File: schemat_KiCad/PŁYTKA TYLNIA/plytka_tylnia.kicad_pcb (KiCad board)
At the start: 2 copper layers, 113.5 x 70.2 mm, 36 parts, among them P1 USB_OTG, SW1 SPST

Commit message: tył do druku
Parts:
- removed BUTTON1: PUSH, warsztatymisc:SW_06_SMD
- removed R4: 10k, Resistors_SMD:R_0805_HandSoldering
- removed R5: 200, Resistors_SMD:R_0805_HandSoldering
- removed SW1: SPST, warsztatymisc:dip_switch_1
- removed SYGNAL_LED1: LED_BLUE, LEDs:LED_0805
- added BOOT0: SWITCH, warsztaty:PRZEŁĄCZNIK_1x3, F.Cu at (94.8, 94.0)
- added Bezpiecznik1: Fuse ??, Fuse_Holders_and_Fuses:Fuse_SMD1206_HandSoldering, B.Cu at (102.4, 87.2)
- added C1: 4,7uF, Capacitors_SMD:C_0805_HandSoldering, F.Cu at (160.9, 74.0)
- added C12: 100nF, Capacitors_SMD:C_0805_HandSoldering, F.Cu at (159.5, 71.8)
- added C15: 10uF, Capacitors_SMD:C_0805_HandSoldering, F.Cu at (113.6, 74.1)
- added C16: 10uF, Capacitors_SMD:C_0805_HandSoldering, F.Cu at (116.8, 64.5)
- added C17: C, Capacitors_SMD:C_0805_HandSoldering, F.Cu at (123.8, 66.9)
- added J1: CONN_01X04, Pin_Headers:Pin_Header_Straight_1x04_Pitch2.00mm, F.Cu at (121.5, 63.3)
- added J2: PIN8, Pin_Headers:Pin_Header_Straight_1x08_Pitch2.00mm, F.Cu at (110.0, 124.0)
- added J3: PIN8, Pin_Headers:Pin_Header_Straight_1x08_Pitch2.00mm, F.Cu at (165.0, 110.0)
- added LED_RGB1: LED_CRGB, warsztaty:LED_RGB_0805, F.Cu at (172.9, 56.9)
- added R10: R, Resistors_SMD:R_0805_HandSoldering, F.Cu at (178.2, 57.0)
- added R11: R, Resistors_SMD:R_0805_HandSoldering, F.Cu at (174.3, 61.1)
- added R12: R, Resistors_SMD:R_0805_HandSoldering, F.Cu at (172.2, 61.1)
- added R13: R, Resistors_SMD:R_0805_HandSoldering, F.Cu at (170.2, 61.1)
- added R7: 51k, Resistors_SMD:R_0805_HandSoldering, B.Cu at (95.8, 82.4)
- added R8: 33k, Resistors_SMD:R_0805_HandSoldering, B.Cu at (94.2, 86.9)
- added REF**: Napęd_tunelowy, Napęd_tunelowy, F.Cu at (137.7, 94.9)
- added REF**: Silnik Pololu, warsztaty:Pololu_silnik, F.Cu at (187.5, 117.5)
- added REF**: Silnik Pololu, warsztaty:Pololu_silnik, F.Cu at (87.5, 117.5)
- added SHARP1: PIN3, Pin_Headers:Pin_Header_Straight_1x03_Pitch2.00mm, F.Cu at (90.0, 73.0)
- added SHARP_RIGHT1: PIN3, Pin_Headers:Pin_Header_Straight_1x03_Pitch2.00mm, F.Cu at (185.0, 69.0)
- added STABILIZATOR2: LM1117DT, warsztaty:LM1117_TO-252, F.Cu at (108.2, 75.9)
- added SWITCH1: Przełącznik_dźwigniowy_podwójny_On-On_MTS, warsztaty:PRZEŁĄCZNIK_2x3, F.Cu at (175.3, 104.7)
- added TURBINA1: PIN3, Pin_Headers:Pin_Header_Straight_1x03_Pitch2.00mm, F.Cu at (91.1, 108.9)
- added Włącznik1: switch, warsztaty:PRZEŁĄCZNIK_1x2, F.Cu at (103.0, 98.8)
- BATERIA1: footprint warsztatymisc:zl_zasilania -> misc:zl_zasilania
- BLUETOOTH1: footprint warsztatymisc:pin_array_4x1 -> Pin_Headers:Pin_Header_Straight_1x04_Pitch2.00mm
- C13, C14, C2, C3, C8, C9, R6, STABILIZATOR1: moved to B.Cu
- C5: footprint warsztatymisc:1206 -> Capacitors_SMD:C_0805_HandSoldering
- C7: footprint warsztatymisc:1210 -> Capacitors_SMD:C_0805_HandSoldering
- MIKROPROCEK1: footprint warsztatymisc:LQFP48 -> misc:LQFP48
- MOTOR_L2, MOTOR_R1: footprint warsztatymisc:silnik -> Pin_Headers:Pin_Header_Straight_1x02_Pitch2.00mm
- P1: footprint warsztatymisc:USB-MINI-B-SMD -> Connectors_USB:USB_Micro-B_Molex-105017-0001
- PRZYCISK_RESET1, START_BUTTON1: footprint warsztatymisc:SW_06_SMD -> misc:SW_06_SMD
- REZONATOR1: footprint warsztatymisc:Kwarc_SMD_Mini -> misc:Kwarc_SMD_Mini; moved to B.Cu
- TRANSISTOR1: footprint warsztatymisc:SOT23-3 -> misc:SOT23-3; moved to B.Cu
- WYJSCIE_DO_PLYTKI_PRZEDNIEJ1: footprint warsztatymisc:fpc_10_pin -> misc:fpc_10_pin
- moved P1 79.5 mm to (94.8, 60.8), turned to 270 degrees
- moved R2 69.3 mm to (100.5, 54.1)
- moved PRZYCISK_RESET1 67.2 mm to (98.7, 87.3)
- moved R3 61.5 mm to (178.9, 79.4), turned to 180 degrees
- moved START_BUTTON1 61.1 mm to (179.7, 86.8), turned to 270 degrees
- moved BLUETOOTH1 55.6 mm to (111.5, 57.8)
- moved C6 52.9 mm to (177.8, 61.8), turned to 0 degrees
- moved BATERIA1 51.4 mm to (120.0, 124.0)
- moved LED_VCC_BATERY1 47.9 mm to (159.9, 56.4), turned to 180 degrees
- moved C13 44.3 mm to (171.5, 79.3)
- moved C14 43.9 mm to (173.9, 79.2)
- moved C10 42.0 mm to (163.1, 78.3)
- moved R1 41.0 mm to (157.4, 60.0), turned to 90 degrees
- moved C11 40.6 mm to (163.7, 80.2)
- moved C9 37.3 mm to (99.5, 76.6)
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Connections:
- BATERIA1 pad 1: Net-(BATERIA1-Pad1) -> GND
- BLUETOOTH1 pad 2: /USART_TX -> /SWCLK
- C2 pad 1: Net-(C3-Pad1) -> Net-(C2-Pad1)
- C3 pad 1: Net-(C2-Pad1) -> Net-(C3-Pad1)
- MIKROPROCEK1 pad 18: Net-(MIKROPROCEK1-Pad45) -> /SHARP_LEFT
- MIKROPROCEK1 pad 19: (no net) -> /LIPOL_POMIAR
- MIKROPROCEK1 pad 2: (no net) -> /LED_R
- MIKROPROCEK1 pad 20: Net-(MIKROPROCEK1-Pad20) -> (no net)
- MIKROPROCEK1 pad 21: (no net) -> /TURBINA_PWM
- MIKROPROCEK1 pad 3: (no net) -> /LED_G
- MIKROPROCEK1 pad 33: (no net) -> Net-(MIKROPROCEK1-Pad33)
- MIKROPROCEK1 pad 38: (no net) -> /USART_RX
- MIKROPROCEK1 pad 39: (no net) -> /SPI1_CLK
- MIKROPROCEK1 pad 4: (no net) -> /LED_B
- MIKROPROCEK1 pad 40: (no net) -> /SPI1_MISO
- MIKROPROCEK1 pad 41: Net-(BUTTON1-Pad2) -> /SPI1_MOSI
- MIKROPROCEK1 pad 42: /USART_RX -> /SPI1_SS1
- MIKROPROCEK1 pad 43: /USART_TX -> /SPI1_SS2
- MIKROPROCEK1 pad 44: (no net) -> /BOOT0
- MIKROPROCEK1 pad 46: (no net) -> /SHARP_RIGHT
- MIKROPROCEK1 pad 5: Net-(C2-Pad1) -> /OSC_IN
- MIKROPROCEK1 pad 6: Net-(C3-Pad1) -> (no net)
- R3 pad 2: Net-(MIKROPROCEK1-Pad20) -> Net-(MIKROPROCEK1-Pad33)
- R6 pad 1: Net-(C8-Pad1) -> /BATERIA
- R6 pad 2: /BATERIA -> Net-(R6-Pad2)
- REZONATOR1 pad 1: Net-(C2-Pad1) -> Net-(C3-Pad1)
- REZONATOR1 pad 2: Net-(C3-Pad1) -> Net-(C2-Pad1)
- START_BUTTON1 pad 2: Net-(MIKROPROCEK1-Pad20) -> Net-(MIKROPROCEK1-Pad33)
- TRANSISTOR1 pad 1: Net-(C8-Pad1) -> GND
- TRANSISTOR1 pad 2: GND -> Net-(R6-Pad2)
- TRANSISTOR1 pad 3: Net-(BATERIA1-Pad1) -> GND
- WYJSCIE_DO_PLYTKI_PRZEDNIEJ1 pad 1: /T8 -> /T1
- WYJSCIE_DO_PLYTKI_PRZEDNIEJ1 pad 2: /T7 -> /T2
- WYJSCIE_DO_PLYTKI_PRZEDNIEJ1 pad 3: /T6 -> /T3
- WYJSCIE_DO_PLYTKI_PRZEDNIEJ1 pad 4: /T5 -> /T4
- WYJSCIE_DO_PLYTKI_PRZEDNIEJ1 pad 5: /T4 -> /T5
- WYJSCIE_DO_PLYTKI_PRZEDNIEJ1 pad 6: /T3 -> /T6
- WYJSCIE_DO_PLYTKI_PRZEDNIEJ1 pad 7: /T2 -> /T7
- WYJSCIE_DO_PLYTKI_PRZEDNIEJ1 pad 8: /T1 -> /T8
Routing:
- net /5V: track 0.00 -> 333.5 mm, vias 0 -> 1
- net GND: track 444.1 -> 156.8 mm, vias 2 -> 1
- net /SPI1_SS1: track 0.00 -> 227.1 mm, vias 0 -> 1
- net VCC: track 205.5 -> 426.5 mm, vias 3 -> 5
- net /SPI1_MISO: track 0.00 -> 186.0 mm, vias 0 -> 2
- net /SPI1_CLK: track 0.00 -> 160.4 mm, vias 0 -> 2
- net /BOOT0: track 0.00 -> 150.0 mm, vias 0 -> 1
- net /SPI1_MOSI: track 0.00 -> 148.8 mm, vias 0 -> 3
- net /BATERIA: track 71.2 -> 219.8 mm, vias 2 -> 3
- net Net-(MOSTEK1-Pad1): track 7.59 -> 135.5 mm, vias 0 -> 1
- net Net-(MOSTEK1-Pad5): track 12.9 -> 128.3 mm, vias 0 -> 3
- net /TURBINA_PWM: track 0.00 -> 99.3 mm, vias 0 -> 2
- net /TRIG: track 0.00 -> 87.2 mm
- net /SHARP_LEFT: track 0.00 -> 84.2 mm, vias 0 -> 4
- net /LIPOL_POMIAR: track 0.00 -> 82.6 mm, vias 0 -> 1
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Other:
- board size 113.5 x 70.2 mm -> 135 x 101 mm
- board text added: "L.F. ANT"
- board text removed: "BEBO"

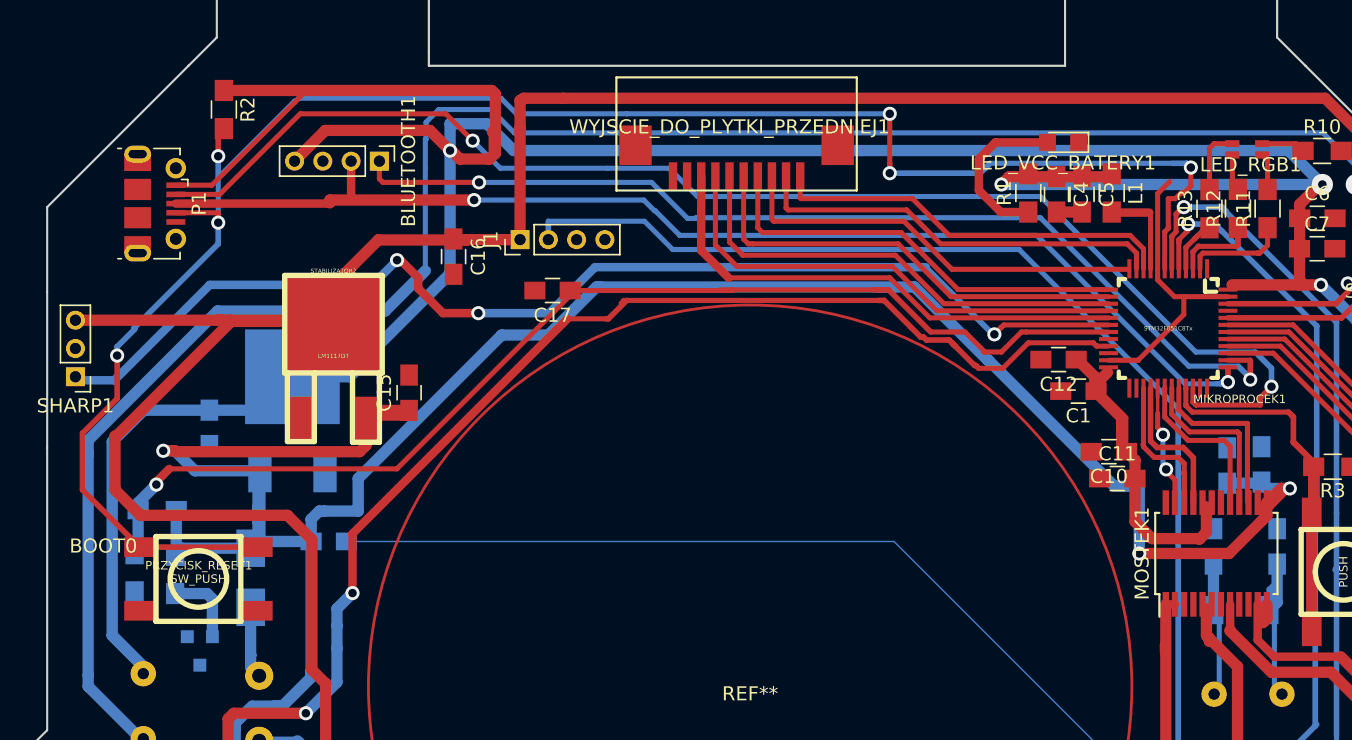
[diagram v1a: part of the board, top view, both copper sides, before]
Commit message: nazwy przyciskow
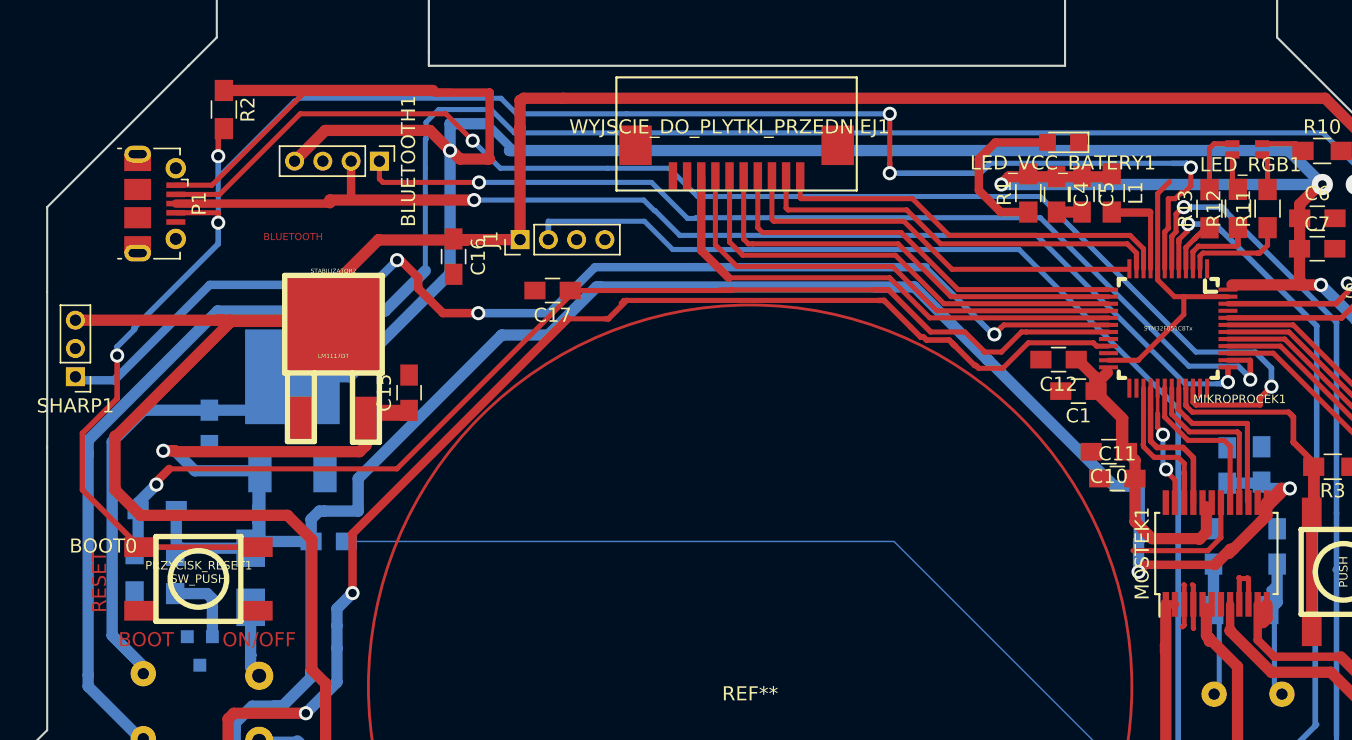
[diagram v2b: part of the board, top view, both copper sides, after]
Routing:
- net GND: track 156.8 -> 176.6 mm
- net VCC: track 426.5 -> 423.3 mm
- net /BATERIA: track 219.8 -> 222.2 mm
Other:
- board text added: "BLUETOOTH"
- board text added: "BOOT"
- board text added: "ON/OFF"
- board text added: "RESET"

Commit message: warstwa dolna okrag
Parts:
- added REF**: Napęd_tunelowy, warsztaty:Napęd_tunelowy, B.Cu at (137.7, 94.9)
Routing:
- net Net-(MOSTEK1-Pad5): track 128.3 -> 138.3 mm
- net Net-(MOSTEK1-Pad1): track 135.5 -> 127.3 mm
- net /5V: track 333.5 -> 331.1 mm
- net /SPI1_CLK: track 160.4 -> 161.2 mm
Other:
- outline, holes or cut-outs redrawn

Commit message: wejscie turbiny tylem
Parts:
- moved TURBINA1 68.9 mm to (157.2, 128.2)
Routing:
- net /ECHO: track 0.14 -> 82.9 mm
- net (no net): track 60.3 -> 108.1 mm
- net /OSC_IN: track 47.8 -> 90.1 mm
- net GND: track 176.6 -> 140.0 mm, vias 1 -> 2
- net /BATERIA: track 222.2 -> 254.4 mm, vias 3 -> 4
- net Net-(MOSTEK1-Pad5): track 138.3 -> 117.9 mm
- net /TURBINA_PWM: track 99.3 -> 80.7 mm
- net /SPI1_MISO: track 186.0 -> 193.2 mm
- net VCC: track 423.3 -> 416.8 mm
- net Net-(C2-Pad1): track 12.6 -> 18.9 mm
- net Net-(C3-Pad1): track 8.94 -> 14.9 mm
- net /TRIG: track 87.2 -> 92.1 mm
- net /SPI1_SS1: track 227.1 -> 222.8 mm
- net Net-(MIKROPROCEK1-Pad33): track 29.5 -> 26.2 mm
- net /SPI1_MOSI: track 148.8 -> 151.3 mm
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
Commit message: poprawiony echo/trig
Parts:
- removed SWITCH1: Przełącznik_dźwigniowy_podwójny_On-On_MTS, warsztaty:PRZEŁĄCZNIK_2x3
- added R14: R, Resistors_SMD:R_0805_HandSoldering, B.Cu at (169.7, 77.5)
- added R15: R, Resistors_SMD:R_0805_HandSoldering, B.Cu at (169.7, 82.4)
- added R4: R, Resistors_SMD:R_0805_HandSoldering, F.Cu at (176.8, 55.9)
- added R5: R, Resistors_SMD:R_0805_HandSoldering, F.Cu at (170.2, 58.2)
- added R9: R, Resistors_SMD:R_0805_HandSoldering, F.Cu at (168.1, 56.1)
- moved BOOT0 74.6 mm to (169.4, 93.9)
- moved REZONATOR1 27.7 mm to (169.5, 61.9)
- moved C2 21.9 mm to (174.9, 63.1), turned to 270 degrees
- moved C3 18.5 mm to (170.7, 66.5), turned to 270 degrees
- moved START_BUTTON1 9.67 mm to (179.0, 96.4)
- moved LED_VCC_BATERY1 9.49 mm to (150.4, 56.4), turned to 0 degrees
- moved C4 7.27 mm to (152.1, 59.7)
- moved L1 7.09 mm to (156.2, 59.9)
- moved R13 7.06 mm to (166.1, 55.4)
- moved C5 7.03 mm to (154.2, 59.7)
- moved R1 4.37 mm to (154.9, 56.4), turned to 0 degrees
- moved R10 4.14 mm to (175.3, 54.1)
- moved LED_RGB1 3.63 mm to (170.9, 53.8)
- moved C9 3.44 mm to (100.1, 73.2)
- moved R12 2.93 mm to (172.2, 58.2)
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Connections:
- MIKROPROCEK1 pad 35: (no net) -> Net-(MIKROPROCEK1-Pad35)
- MIKROPROCEK1 pad 36: (no net) -> /TRIG
- MIKROPROCEK1 pad 5: /OSC_IN -> Net-(C2-Pad1)
- MIKROPROCEK1 pad 6: (no net) -> Net-(C3-Pad1)
- R13 pad 1: /LED_B -> GND
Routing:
- net /BOOT0: track 150.0 -> 42.1 mm
- net /OSC_IN: track 90.1 -> 0.00 mm, vias 1 -> 0
- net (no net): track 108.1 -> 19.1 mm, vias 1 -> 0
- net GND: track 140.0 -> 223.5 mm, vias 2 -> 0
- net VCC: track 416.8 -> 368.0 mm, vias 5 -> 7
- net /ECHO: track 82.9 -> 52.9 mm
- net /TRIG: track 92.1 -> 64.4 mm, vias 0 -> 1
- net /BATERIA: track 254.4 -> 278.2 mm, vias 4 -> 5
- net /SWCLK: track 108.4 -> 87.6 mm
- net /5V: track 330.8 -> 351.4 mm
- net Net-(MOSTEK1-Pad11): track 33.0 -> 20.9 mm
- net Net-(MIKROPROCEK1-Pad35): track 0.00 -> 11.5 mm, vias 0 -> 1
- net Net-(MOSTEK1-Pad7): track 32.7 -> 21.4 mm
- net Net-(LED_VCC_BATERY1-Pad2): track 11.7 -> 2.07 mm
- net /RESET: track 132.5 -> 123.6 mm, vias 6 -> 4
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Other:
- board text added: "START"

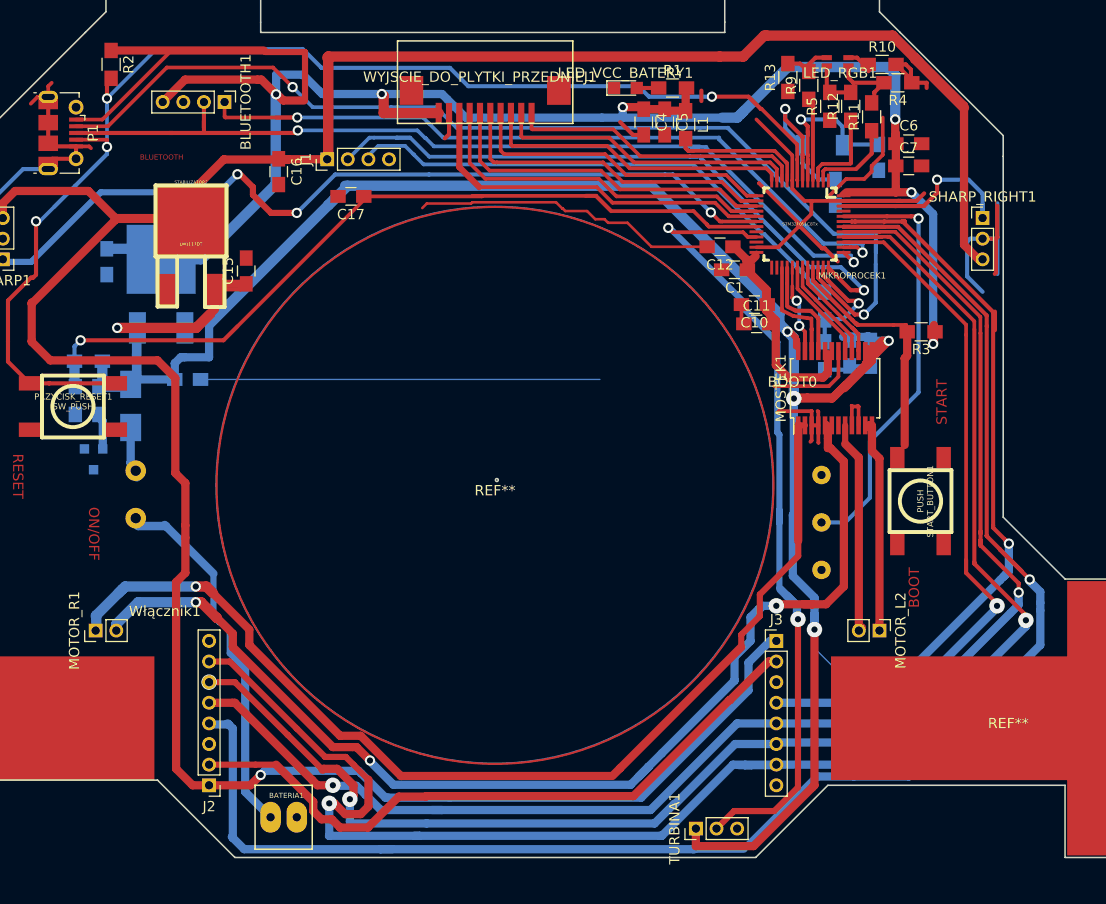
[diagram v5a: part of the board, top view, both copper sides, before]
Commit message: Usuniecie zlacza 3x2
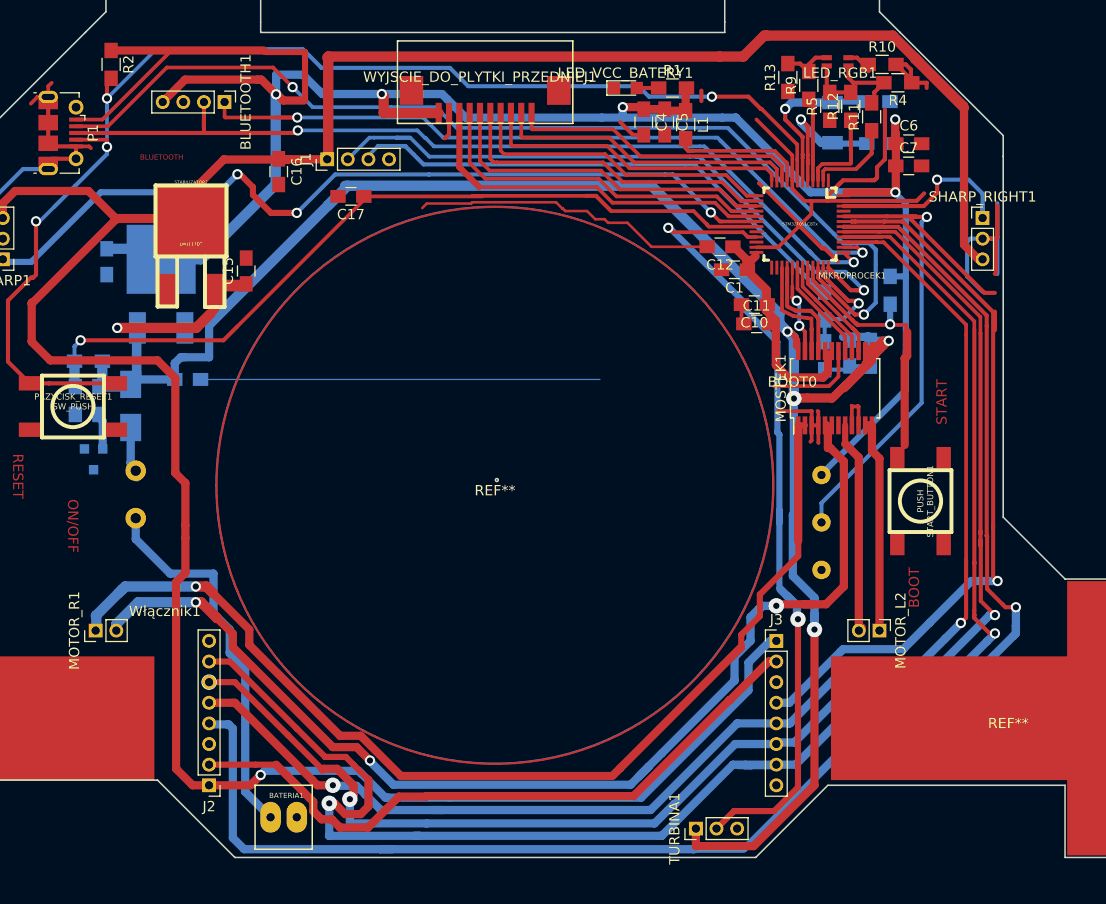
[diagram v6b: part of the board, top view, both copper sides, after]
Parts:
- R3: moved to B.Cu
- moved C3 9.68 mm to (174.8, 57.7), turned to 0 degrees
- moved R3 5.02 mm to (176.0, 76.0), turned to 270 degrees
- moved REZONATOR1 2.40 mm to (170.4, 59.7), turned to 90 degrees
- moved C2 1.34 mm to (175.0, 61.8), turned to 0 degrees
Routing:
- net /SPI1_MISO: track 196.5 -> 162.8 mm
- net /SPI1_CLK: track 160.2 -> 140.8 mm
- net (no net): track 19.1 -> 1.21 mm
- net GND: track 223.5 -> 237.1 mm
- net /BOOT0: track 42.1 -> 53.9 mm
- net /SPI1_MOSI: track 151.2 -> 140.0 mm
- net /SPI1_SS2: track 82.1 -> 72.4 mm
- net VCC: track 368.0 -> 375.4 mm, vias 7 -> 6
- net /ECHO: track 52.9 -> 59.9 mm
- net /SPI1_SS1: track 222.4 -> 216.3 mm
- net Net-(MIKROPROCEK1-Pad33): track 26.4 -> 28.5 mm, vias 0 -> 1
- net Net-(C2-Pad1): track 16.9 -> 14.8 mm
- net Net-(C3-Pad1): track 17.5 -> 15.7 mm
- net /SWDIO: track 102.9 -> 101.9 mm
- net /TRIG: track 64.4 -> 63.7 mm
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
